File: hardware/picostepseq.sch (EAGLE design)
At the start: 27 parts, among them J1 SJ-3523-SMT, J2 SJ-3523-SMT, SW1 LED_SWITCHSTEP, SW2 LED_SWITCHSTEP, SW3 LED_SWITCHSTEP, SW4 LED_SWITCHSTEP, SW5 LED_SWITCHSTEP, SW6 LED_SWITCHSTEP, SW7 LED_SWITCHSTEP, SW8 LED_SWITCHSTEP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

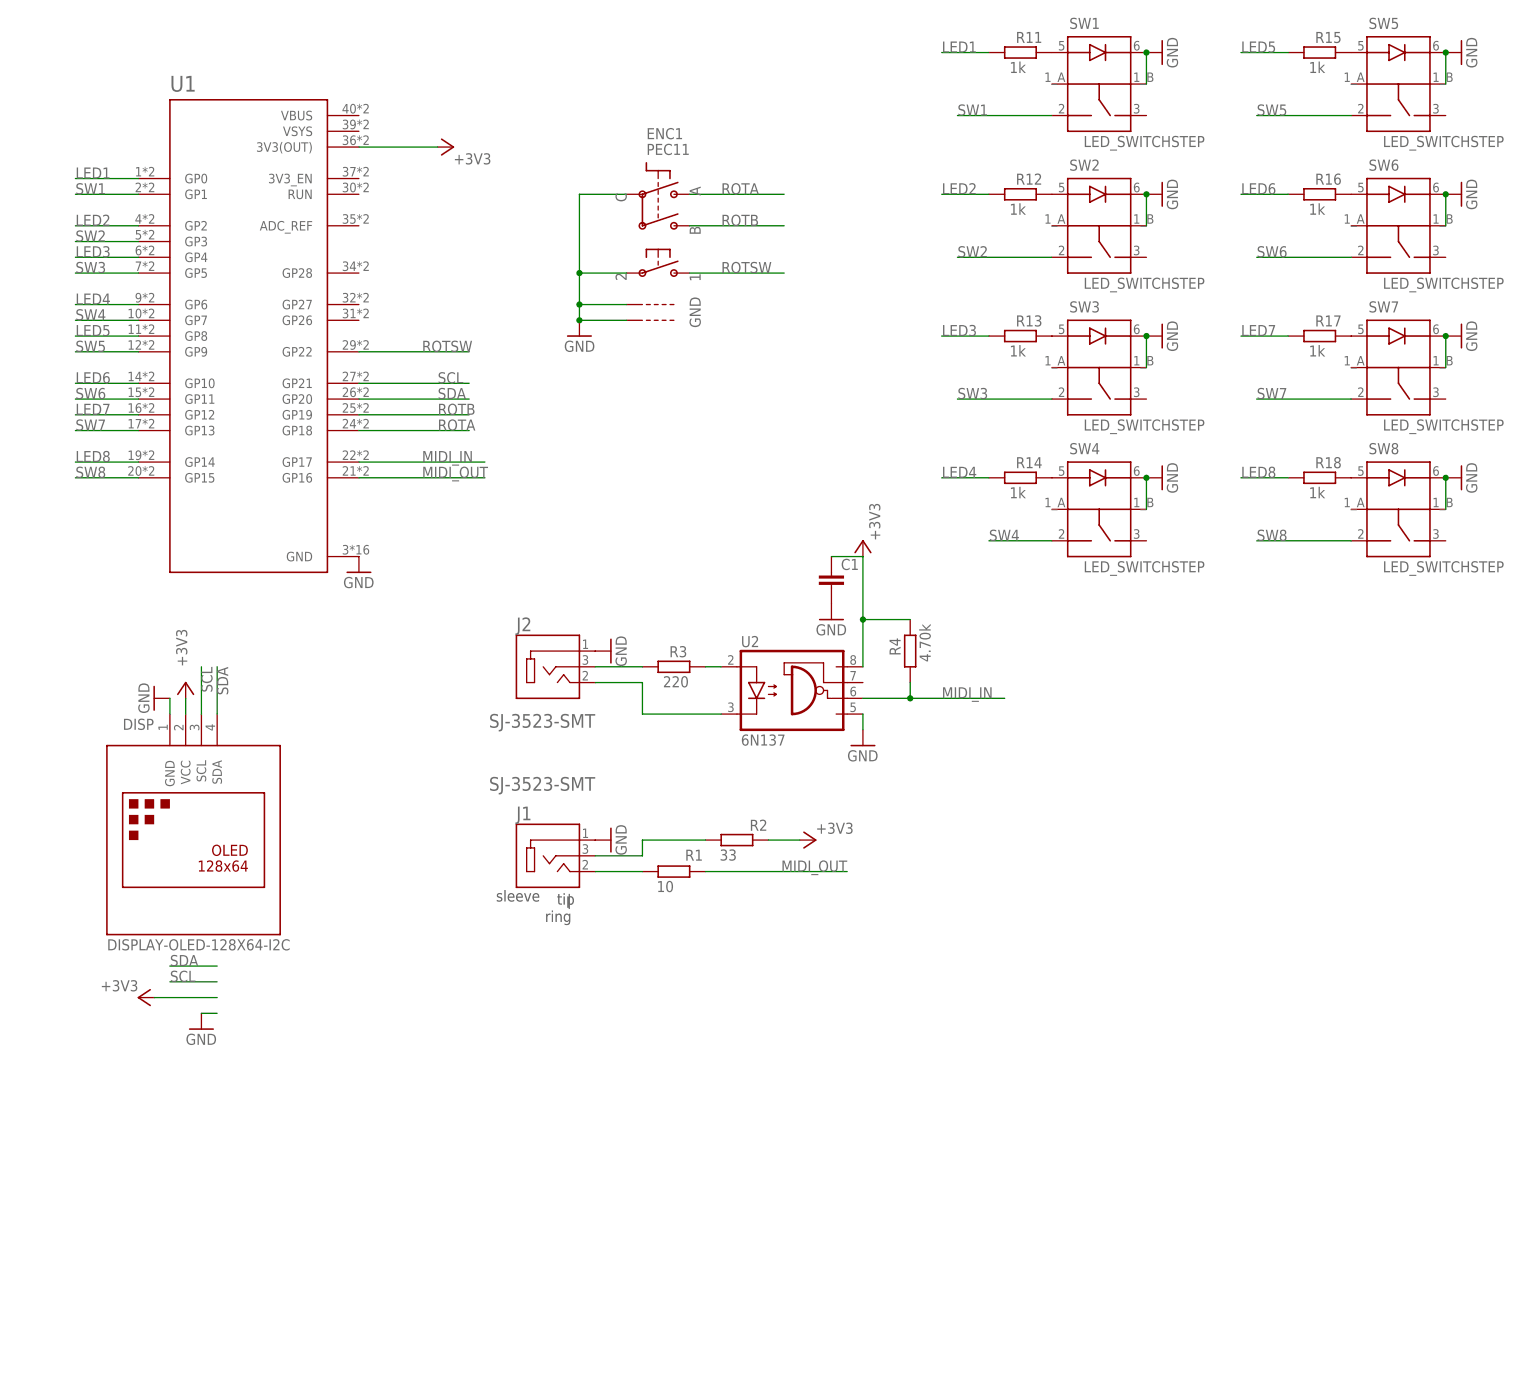
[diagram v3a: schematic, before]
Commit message: update readme with bom
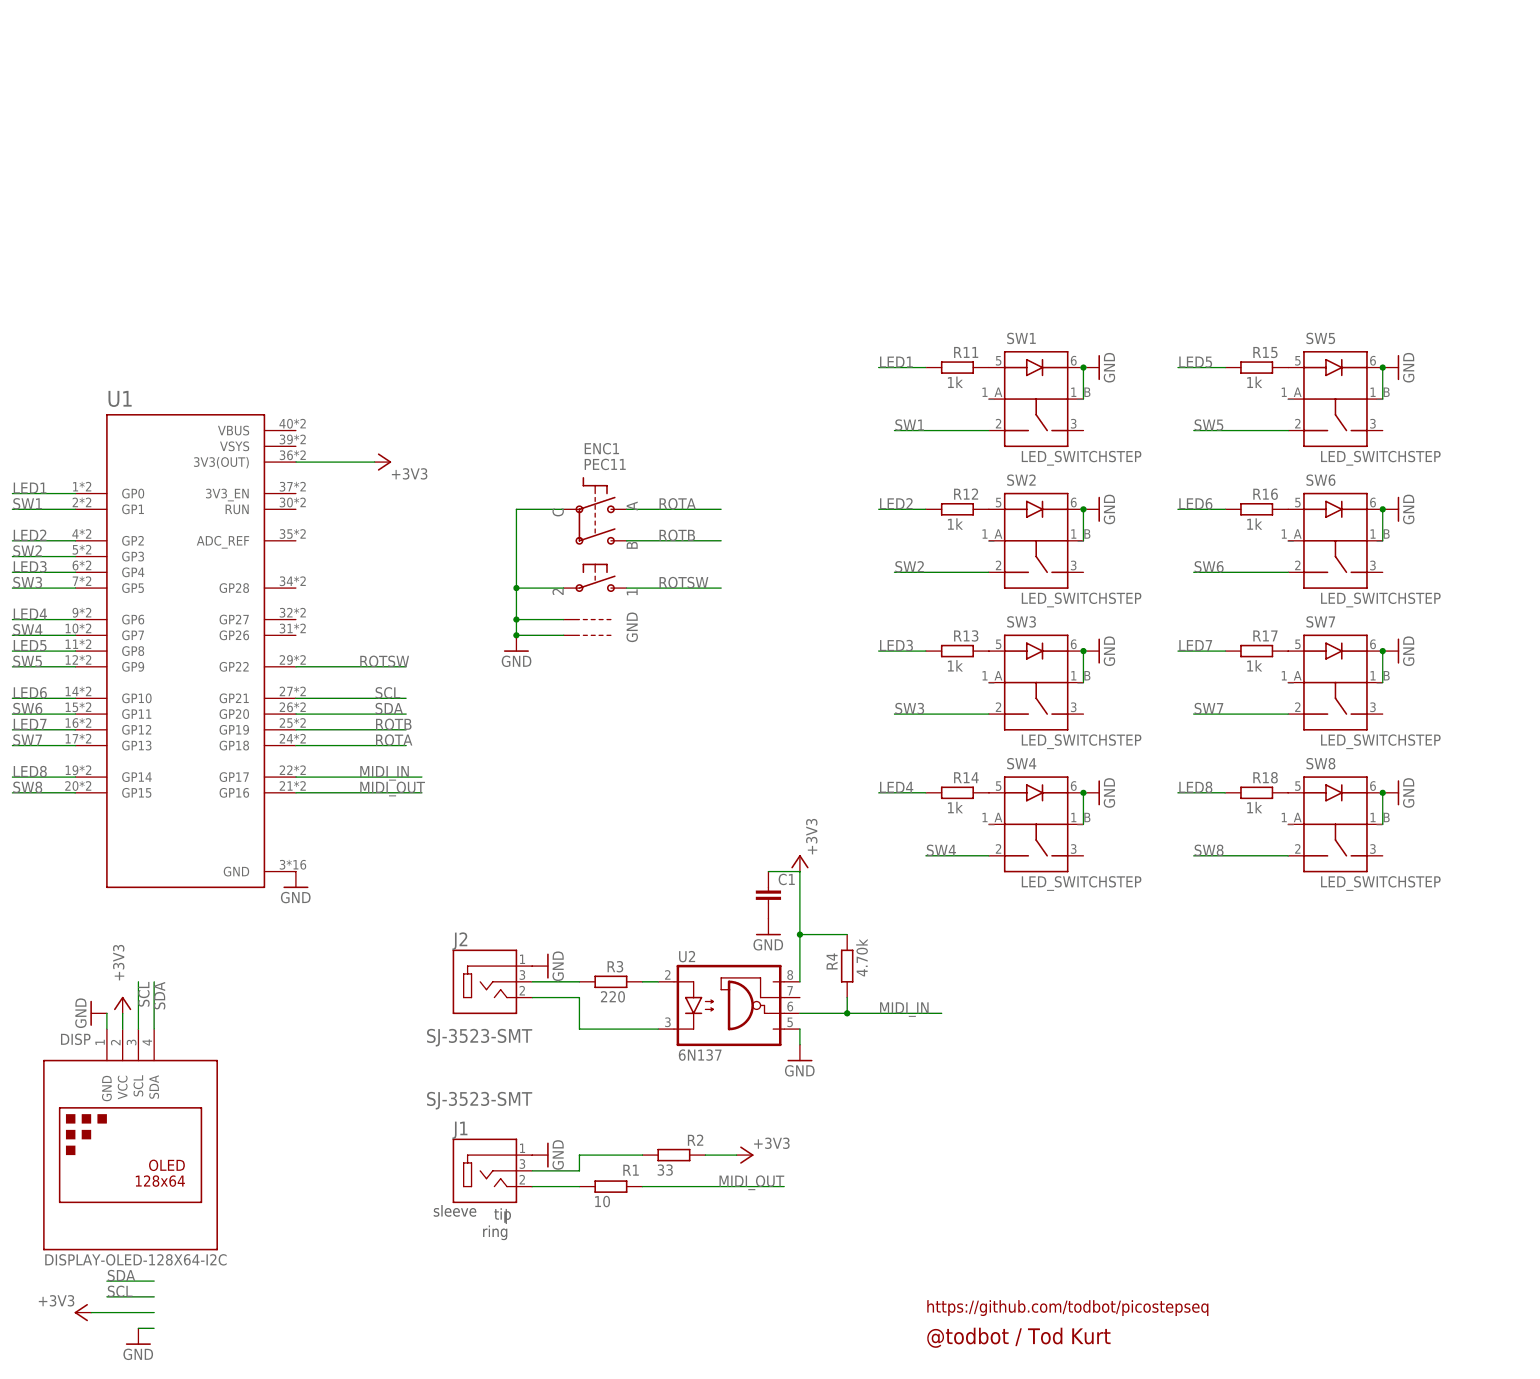
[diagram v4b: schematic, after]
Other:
- note added: "@todbot / Tod Kurt"
- note added: "https://github.com/todbot/picostepseq"
- moved on the sheet: C1, DISP, ENC1, J1, J2, R1, R11, R12, R13, R14, R15, R16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
